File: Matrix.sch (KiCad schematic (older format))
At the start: 227 parts

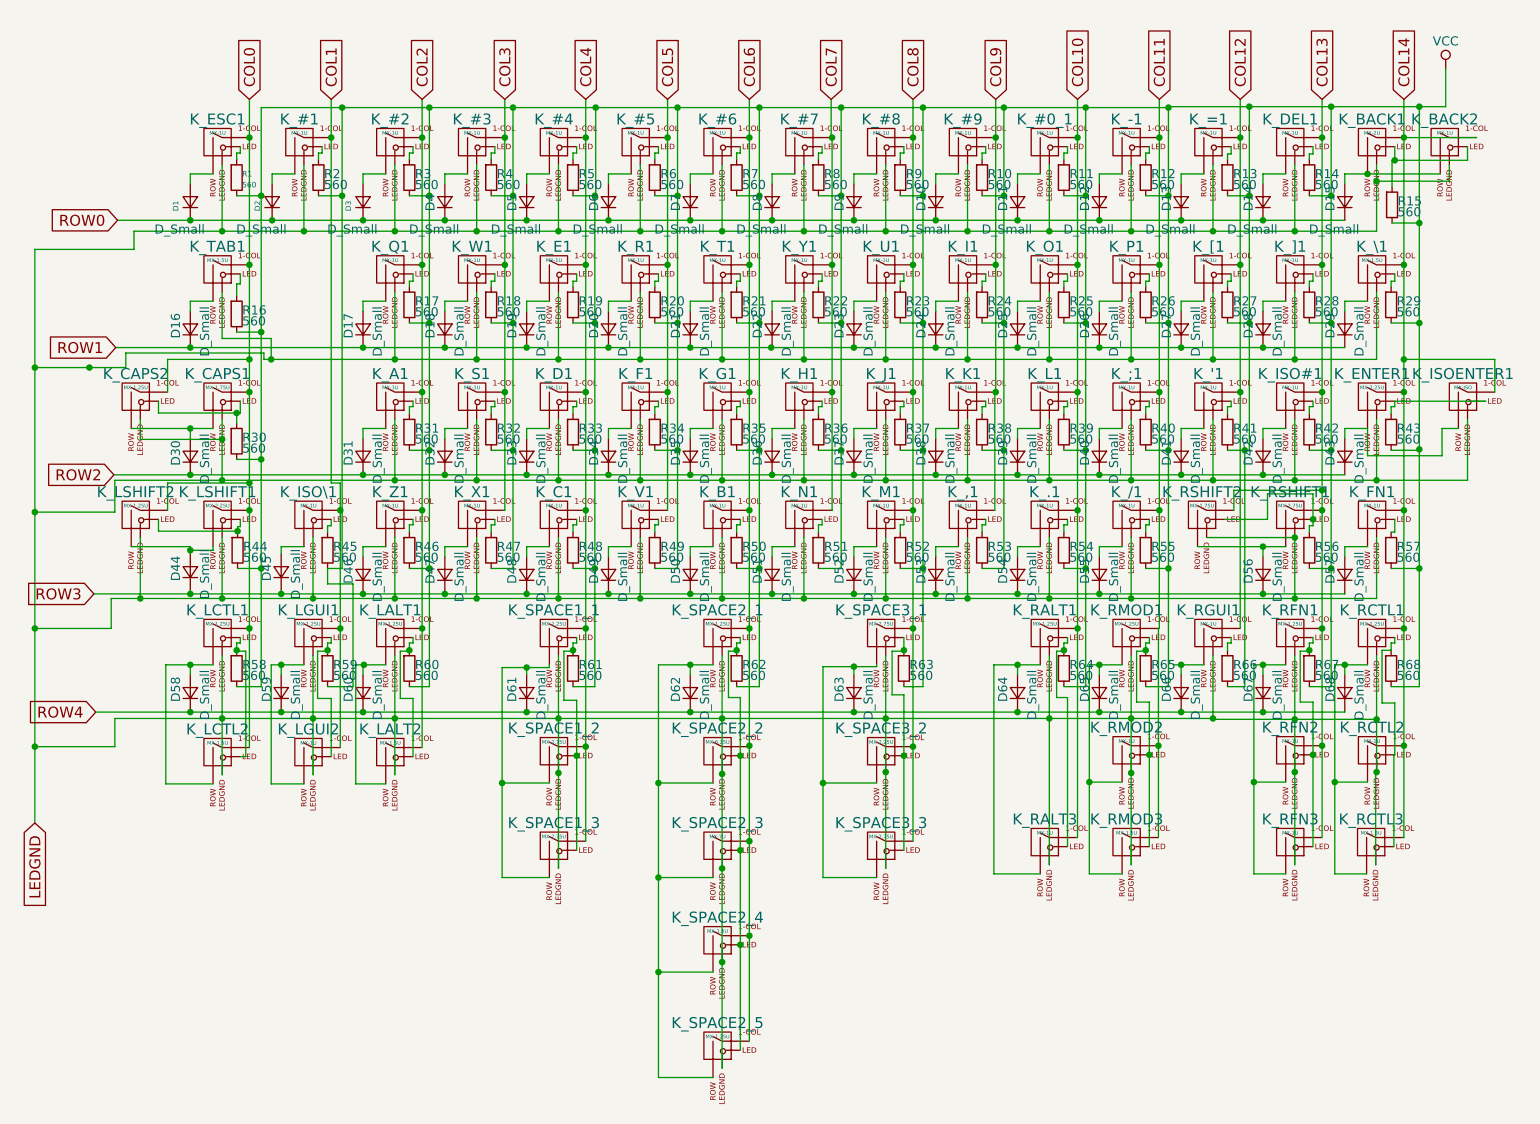
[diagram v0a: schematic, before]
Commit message: Update: Work on moving resistors in schematic. Not done yet.
I've got the top three rows done so far.
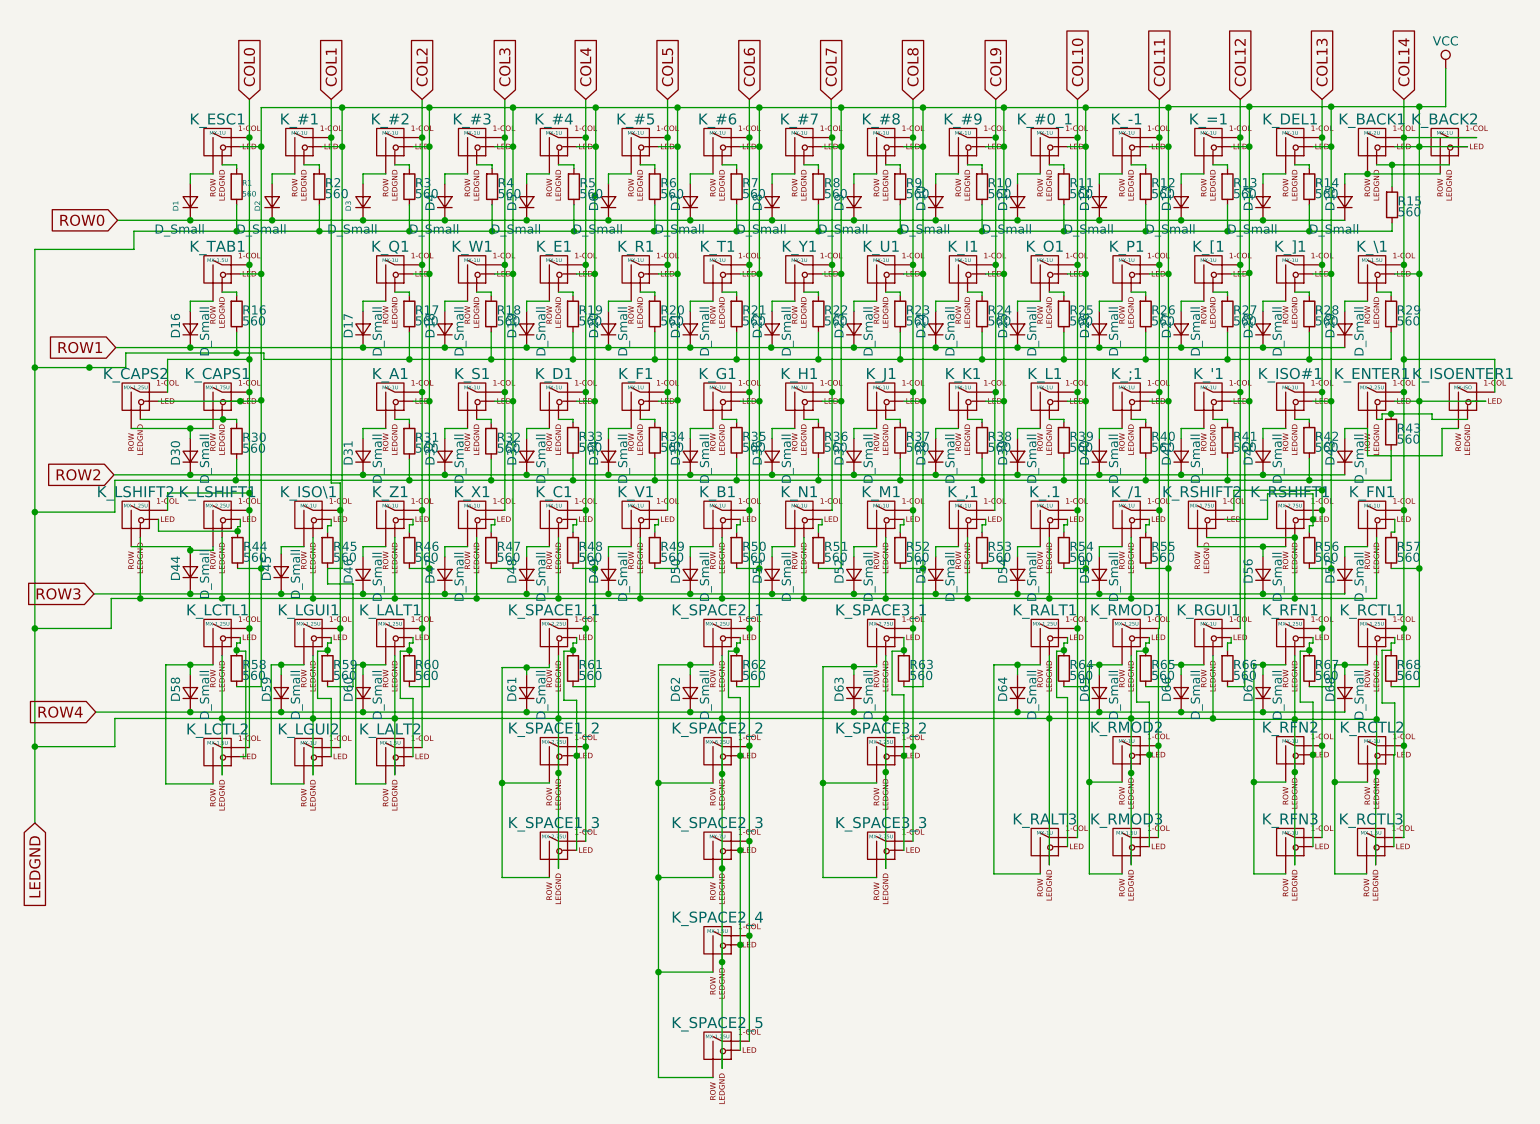
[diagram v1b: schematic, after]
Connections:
- net LEDGND: now also R1.2, R10.2, R11.2, R12.2, R13.2, R14.2, R15.2, R16.2, R17.2, R18.2, R19.2, R2.2, R20.2, R21.2, R22.2, R23.2, R24.2, R25.2, R26.2, R27.2, R28.2, R29.2, R3.2, R30.2, R31.2, R32.2, R33.2, R34.2, R35.2, R36.2, R37.2, R38.2, R39.2, R4.2, R40.2, R41.2, R42.2, R43.2, R5.2, R6.2, R7.2, R8.2, R9.2; no longer K_#0_1.4 (LEDGND), K_#1.4 (LEDGND), K_#2.4 (LEDGND), K_#3.4 (LEDGND), K_#4.4 (LEDGND), K_#5.4 (LEDGND), K_#6.4 (LEDGND), K_#7.4 (LEDGND), K_#8.4 (LEDGND), K_#9.4 (LEDGND), K_'1.4 (LEDGND), K_-1.4 (LEDGND), K_;1.4 (LEDGND), K_=1.4 (LEDGND), K_A1.4 (LEDGND), K_BACK1.4 (LEDGND), K_BACK2.4 (LEDGND), K_CAPS1.4 (LEDGND), K_CAPS2.4 (LEDGND), K_D1.4 (LEDGND), K_DEL1.4 (LEDGND), K_E1.4 (LEDGND), K_ENTER1.4 (LEDGND), K_ESC1.4 (LEDGND), K_F1.4 (LEDGND), K_G1.4 (LEDGND), K_H1.4 (LEDGND), K_I1.4 (LEDGND), K_ISO#1.4 (LEDGND), K_ISOENTER1.4 (LEDGND), K_J1.4 (LEDGND), K_K1.4 (LEDGND), K_L1.4 (LEDGND), K_O1.4 (LEDGND), K_P1.4 (LEDGND), K_Q1.4 (LEDGND), K_R1.4 (LEDGND), K_S1.4 (LEDGND), K_T1.4 (LEDGND), K_TAB1.4 (LEDGND), K_U1.4 (LEDGND), K_W1.4 (LEDGND), K_Y1.4 (LEDGND), K_[1.4 (LEDGND), K_\1.4 (LEDGND), K_]1.4 (LEDGND)
- net VCC: now also K_#0_1.3 (LED), K_#1.3 (LED), K_#2.3 (LED), K_#3.3 (LED), K_#4.3 (LED), K_#5.3 (LED), K_#6.3 (LED), K_#7.3 (LED), K_#8.3 (LED), K_#9.3 (LED), K_'1.3 (LED), K_-1.3 (LED), K_;1.3 (LED), K_=1.3 (LED), K_A1.3 (LED), K_BACK1.3 (LED), K_BACK2.3 (LED), K_CAPS1.3 (LED), K_CAPS2.3 (LED), K_DEL1.3 (LED), K_ENTER1.3 (LED), K_ESC1.3 (LED), K_F1.3 (LED), K_G1.3 (LED), K_H1.3 (LED), K_I1.3 (LED), K_ISO#1.3 (LED), K_ISOENTER1.3 (LED), K_J1.3 (LED), K_K1.3 (LED), K_L1.3 (LED), K_O1.3 (LED), K_P1.3 (LED), K_Q1.3 (LED), K_R1.3 (LED), K_S1.3 (LED), K_T1.3 (LED), K_TAB1.3 (LED), K_U1.3 (LED), K_W1.3 (LED), K_Y1.3 (LED), K_[1.3 (LED), K_\1.3 (LED), K_]1.3 (LED); no longer R1.2, R10.2, R11.2, R12.2, R13.2, R14.2, R15.2, R16.2, R17.2, R18.2, R19.2, R2.2, R20.2, R21.2, R22.2, R23.2, R24.2, R25.2, R26.2, R27.2, R28.2, R29.2, R3.2, R30.2, R31.2, R32.2, R33.2, R34.2, R35.2, R36.2, R37.2, R38.2, R39.2, R4.2, R40.2, R41.2, R42.2, R43.2, R48.2, R5.2, R6.2, R61.2, R7.2, R8.2, R9.2
- net at R1.1: now also K_ESC1.4 (LEDGND); no longer K_ESC1.3 (LED)
- net at R2.1: now also K_#1.4 (LEDGND); no longer K_#1.3 (LED)
- net at R3.1: now also K_#2.4 (LEDGND); no longer K_#2.3 (LED)
- net at R4.1: now also K_#3.4 (LEDGND); no longer K_#3.3 (LED)
- net at R5.1: now also K_#4.4 (LEDGND); no longer K_#4.3 (LED)
- net at R6.1: now also K_#5.4 (LEDGND); no longer K_#5.3 (LED)
- net at R7.1: now also K_#6.4 (LEDGND); no longer K_#6.3 (LED)
- net at R8.1: now also K_#7.4 (LEDGND); no longer K_#7.3 (LED)
- net at R9.1: now also K_#8.4 (LEDGND); no longer K_#8.3 (LED)
- net at R10.1: now also K_#9.4 (LEDGND); no longer K_#9.3 (LED)
- net at R11.1: now also K_#0_1.4 (LEDGND); no longer K_#0_1.3 (LED)
- net at R12.1: now also K_-1.4 (LEDGND); no longer K_-1.3 (LED)
- net at R13.1: now also K_=1.4 (LEDGND); no longer K_=1.3 (LED)
- net at R14.1: now also K_DEL1.4 (LEDGND); no longer K_DEL1.3 (LED)
- net at R16.1: now also K_TAB1.4 (LEDGND); no longer K_TAB1.3 (LED)
- net at R17.1: now also K_Q1.4 (LEDGND); no longer K_Q1.3 (LED)
- net at R18.1: now also K_W1.4 (LEDGND); no longer K_W1.3 (LED)
- net at K_E1.3 (LED): now also K_D1.3 (LED), R48.2, R61.2; no longer R19.1
- net at R20.1: now also K_R1.4 (LEDGND); no longer K_R1.3 (LED)
- net at R21.1: now also K_T1.4 (LEDGND); no longer K_T1.3 (LED)
- net at R22.1: now also K_Y1.4 (LEDGND); no longer K_Y1.3 (LED)
- net at R23.1: now also K_U1.4 (LEDGND); no longer K_U1.3 (LED)
- net at R24.1: now also K_I1.4 (LEDGND); no longer K_I1.3 (LED)
- net at R25.1: now also K_O1.4 (LEDGND); no longer K_O1.3 (LED)
- net at R26.1: now also K_P1.4 (LEDGND); no longer K_P1.3 (LED)
- net at R27.1: now also K_[1.4 (LEDGND); no longer K_[1.3 (LED)
- net at R28.1: now also K_]1.4 (LEDGND); no longer K_]1.3 (LED)
- net at R29.1: now also K_\1.4 (LEDGND); no longer K_\1.3 (LED)
- net at R31.1: now also K_A1.4 (LEDGND); no longer K_A1.3 (LED)
- net at R32.1: now also K_S1.4 (LEDGND); no longer K_S1.3 (LED)
- net at R33.1: now also K_D1.4 (LEDGND); no longer K_D1.3 (LED)
- net at R34.1: now also K_F1.4 (LEDGND); no longer K_F1.3 (LED)
- net at R35.1: now also K_G1.4 (LEDGND); no longer K_G1.3 (LED)
- net at R36.1: now also K_H1.4 (LEDGND); no longer K_H1.3 (LED)
- net at R37.1: now also K_J1.4 (LEDGND); no longer K_J1.3 (LED)
- net at R38.1: now also K_K1.4 (LEDGND); no longer K_K1.3 (LED)
- net at R39.1: now also K_L1.4 (LEDGND); no longer K_L1.3 (LED)
- net at R40.1: now also K_;1.4 (LEDGND); no longer K_;1.3 (LED)
- net at R41.1: now also K_'1.4 (LEDGND); no longer K_'1.3 (LED)
- net at R42.1: now also K_ISO#1.4 (LEDGND); no longer K_ISO#1.3 (LED)
- new net: K_BACK1.4 (LEDGND), K_BACK2.4 (LEDGND), R15.1
- new net: K_E1.4 (LEDGND), R19.1
- new net: K_CAPS1.4 (LEDGND), K_CAPS2.4 (LEDGND), R30.1
- new net: K_ENTER1.4 (LEDGND), K_ISOENTER1.4 (LEDGND), R43.1
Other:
- moved on the sheet: R1, R10, R11, R12, R13, R14, R17, R18, R19, R2, R20, R21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

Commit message: Update: Finish moving resistors to ground side
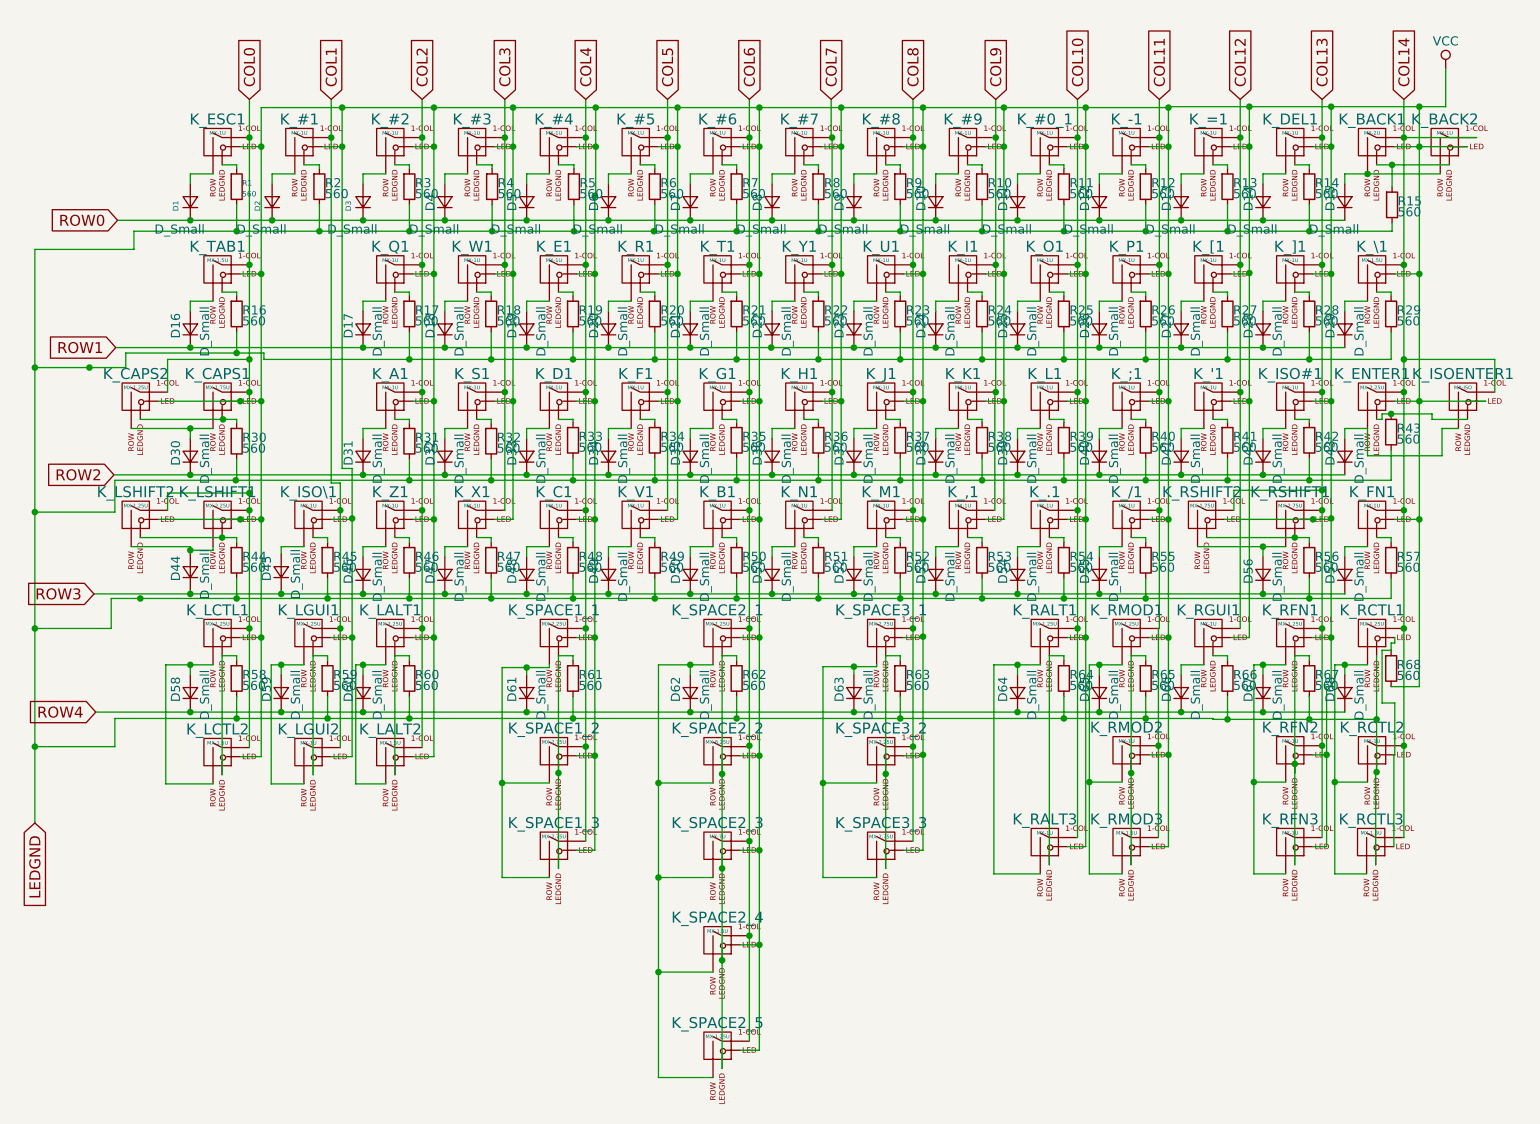
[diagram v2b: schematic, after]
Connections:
- net LEDGND: now also R44.2, R45.2, R46.2, R47.2, R48.2, R49.2, R50.2, R51.2, R52.2, R53.2, R54.2, R55.2, R56.2, R57.2, R58.2, R59.2, R60.2, R61.2, R62.2, R63.2, R64.2, R65.2, R66.2, R67.2; no longer K_,1.4 (LEDGND), K_.1.4 (LEDGND), K_/1.4 (LEDGND), K_B1.4 (LEDGND), K_C1.4 (LEDGND), K_FN1.4 (LEDGND), K_ISO\1.4 (LEDGND), K_LALT1.4 (LEDGND), K_LALT2.4 (LEDGND), K_LCTL1.4 (LEDGND), K_LCTL2.4 (LEDGND), K_LGUI1.4 (LEDGND), K_LGUI2.4 (LEDGND), K_LSHIFT1.4 (LEDGND), K_LSHIFT2.4 (LEDGND), K_M1.4 (LEDGND), K_N1.4 (LEDGND), K_RALT1.4 (LEDGND), K_RALT3.4 (LEDGND), K_RFN1.4 (LEDGND), K_RFN2.4 (LEDGND), K_RFN3.4 (LEDGND), K_RGUI1.4 (LEDGND), K_RMOD1.4 (LEDGND), K_RMOD2.4 (LEDGND), K_RMOD3.4 (LEDGND), K_RSHIFT1.4 (LEDGND), K_RSHIFT2.4 (LEDGND), K_SPACE1_1.4 (LEDGND), K_SPACE1_2.4 (LEDGND), K_SPACE1_3.4 (LEDGND), K_SPACE2_1.4 (LEDGND), K_SPACE2_2.4 (LEDGND), K_SPACE2_3.4 (LEDGND), K_SPACE2_4.4 (LEDGND), K_SPACE2_5.4 (LEDGND), K_SPACE3_1.4 (LEDGND), K_SPACE3_2.4 (LEDGND), K_SPACE3_3.4 (LEDGND), K_V1.4 (LEDGND), K_X1.4 (LEDGND), K_Z1.4 (LEDGND)
- net VCC: now also K_,1.3 (LED), K_.1.3 (LED), K_/1.3 (LED), K_B1.3 (LED), K_FN1.3 (LED), K_ISO\1.3 (LED), K_LALT1.3 (LED), K_LALT2.3 (LED), K_LCTL1.3 (LED), K_LCTL2.3 (LED), K_LGUI1.3 (LED), K_LGUI2.3 (LED), K_LSHIFT1.3 (LED), K_LSHIFT2.3 (LED), K_M1.3 (LED), K_N1.3 (LED), K_RALT1.3 (LED), K_RALT3.3 (LED), K_RFN1.3 (LED), K_RFN2.3 (LED), K_RFN3.3 (LED), K_RGUI1.3 (LED), K_RMOD1.3 (LED), K_RMOD2.3 (LED), K_RMOD3.3 (LED), K_RSHIFT1.3 (LED), K_RSHIFT2.3 (LED), K_SPACE2_1.3 (LED), K_SPACE2_2.3 (LED), K_SPACE2_3.3 (LED), K_SPACE2_4.3 (LED), K_SPACE2_5.3 (LED), K_SPACE3_1.3 (LED), K_SPACE3_2.3 (LED), K_SPACE3_3.3 (LED), K_V1.3 (LED), K_X1.3 (LED), K_Z1.3 (LED); no longer R44.2, R45.2, R46.2, R47.2, R49.2, R50.2, R51.2, R52.2, R53.2, R54.2, R55.2, R56.2, R57.2, R58.2, R59.2, R60.2, R62.2, R63.2, R64.2, R65.2, R66.2, R67.2
- net at K_D1.3 (LED), K_E1.3 (LED): now also K_C1.3 (LED), K_SPACE1_1.3 (LED), K_SPACE1_2.3 (LED), K_SPACE1_3.3 (LED); no longer R48.2, R61.2
- net at R45.1: now also K_ISO\1.4 (LEDGND); no longer K_ISO\1.3 (LED)
- net at R46.1: now also K_Z1.4 (LEDGND); no longer K_Z1.3 (LED)
- net at R47.1: now also K_X1.4 (LEDGND); no longer K_X1.3 (LED)
- net at R48.1: now also K_C1.4 (LEDGND); no longer K_C1.3 (LED)
- net at R49.1: now also K_V1.4 (LEDGND); no longer K_V1.3 (LED)
- net at R50.1: now also K_B1.4 (LEDGND); no longer K_B1.3 (LED)
- net at R51.1: now also K_N1.4 (LEDGND); no longer K_N1.3 (LED)
- net at R52.1: now also K_M1.4 (LEDGND); no longer K_M1.3 (LED)
- net at R53.1: now also K_,1.4 (LEDGND); no longer K_,1.3 (LED)
- net at R54.1: now also K_.1.4 (LEDGND); no longer K_.1.3 (LED)
- net at R55.1: now also K_/1.4 (LEDGND); no longer K_/1.3 (LED)
- net at R57.1: now also K_FN1.4 (LEDGND); no longer K_FN1.3 (LED)
- net at R66.1: now also K_RGUI1.4 (LEDGND); no longer K_RGUI1.3 (LED)
- new net: K_LSHIFT1.4 (LEDGND), K_LSHIFT2.4 (LEDGND), R44.1
- new net: K_RSHIFT1.4 (LEDGND), K_RSHIFT2.4 (LEDGND), R56.1
- new net: K_LCTL1.4 (LEDGND), K_LCTL2.4 (LEDGND), R58.1
- new net: K_LGUI1.4 (LEDGND), K_LGUI2.4 (LEDGND), R59.1
- new net: K_LALT1.4 (LEDGND), K_LALT2.4 (LEDGND), R60.1
- new net: K_SPACE1_1.4 (LEDGND), K_SPACE1_2.4 (LEDGND), K_SPACE1_3.4 (LEDGND), R61.1
- new net: K_SPACE2_1.4 (LEDGND), K_SPACE2_2.4 (LEDGND), K_SPACE2_3.4 (LEDGND), K_SPACE2_4.4 (LEDGND), K_SPACE2_5.4 (LEDGND), R62.1
- new net: K_SPACE3_1.4 (LEDGND), K_SPACE3_2.4 (LEDGND), K_SPACE3_3.4 (LEDGND), R63.1
- new net: K_RALT1.4 (LEDGND), K_RALT3.4 (LEDGND), R64.1
- new net: K_RMOD1.4 (LEDGND), K_RMOD2.4 (LEDGND), K_RMOD3.4 (LEDGND), R65.1
- new net: K_RFN1.4 (LEDGND), K_RFN2.4 (LEDGND), K_RFN3.4 (LEDGND), R67.1
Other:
- moved on the sheet: R44, R45, R46, R47, R48, R49, R50, R51, R52, R53, R54, R55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

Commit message: Update: Switch to Amphenol USB C connector
This connector seems more readily available than the Wurth,
and is about half the price.
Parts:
- K_ISOENTER1: footprint MX_Alps_Hybrid:MXOnly-ISO-ReversedStabilizers -> MX_Alps_Hybrid:MXOnly-ISO-ROTATED-ReversedStabilizers
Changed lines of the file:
@@
 F 0 "K_ISOENTER1" H 8400 2625 60  0000 C CNN
 F 1 "MX-ISO" H 8400 2550 20  0000 C CNN
-F 2 "MX_Alps_Hybrid:MXOnly-ISO-ReversedStabilizers" H 8375 2475 60  0001 C CNN
+F 2 "MX_Alps_Hybrid:MXOnly-ISO-ROTATED-ReversedStabilizers" H 8375 2475 60  0001 C CNN
 F 3 "" H 8375 2475 60  0001 C CNN
 	1    8400 2500

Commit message: Update: Choose more components, lock switch footprints, place some resistors and diodes
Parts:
- D1: Product (none) -> 1N4148W-TP
- R1: Product (none) -> MCT06030C5600FP500
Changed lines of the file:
@@
 F 1 "D_Small" V 1250 1350 50  0000 L CNN
 F 2 "Diodes_SMD:D_SOD-123" V 1400 1430 50  0001 C CNN
-F 3 "" V 1400 1430 50  0001 C CNN
+F 3 "http://www.mccsemi.com/up_pdf/1N4148W(SOD123).pdf" V 1400 1430 50  0001 C CNN
+F 4 "1N4148W-TP" H 1400 1430 60  0001 C CNN "Product"
 	1    1400 1430
 	0    -1   -1   0
@@
 F 2 "Resistors_SMD:R_0603" H 1655 1345 50  0001 C CNN
 F 3 "" H 1655 1345 50  0001 C CNN
+F 4 "MCT06030C5600FP500" H 1655 1345 60  0001 C CNN "Product"
 	1    1655 1345
 	1    0    0    -1

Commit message: Update: Flip LED orientation on most switch footprints
I'm hoping this will separate the diodes and resistors
a little more and make routing easier.
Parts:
- K_#0_1, K_#1, K_#2, K_#3, K_#4, K_#5, K_#6, K_#7, K_#8, K_#9, K_'1, K_,1, K_-1, K_.1, K_/1, K_;1, K_=1, K_A1, K_B1, K_BACK2, K_C1, K_D1, K_DEL1, K_E1, K_ESC1, K_F1, K_FN1, K_G1, K_H1, K_I1, K_ISO#1, K_ISO\1, K_J1, K_K1, K_L1, K_M1, K_N1, K_O1, K_P1, K_Q1, K_R1, K_RGUI1, K_S1, K_T1, K_U1, K_V1, K_W1, K_X1, K_Y1, K_Z1, K_[1, K_]1: footprint MX_Alps_Hybrid:MXOnly-1U -> MX_Alps_Hybrid:MXOnly-1U-FLIPPED
- K_BACK1: footprint MX_Alps_Hybrid:MXOnly-2U -> MX_Alps_Hybrid:MXOnly-2U-FLIPPED
- K_ENTER1, K_LSHIFT1: footprint MX_Alps_Hybrid:MXOnly-2.25U -> MX_Alps_Hybrid:MXOnly-2.25U-FLIPPED
- K_LSHIFT2: footprint MX_Alps_Hybrid:MXOnly-1.25U -> MX_Alps_Hybrid:MXOnly-1.25U-FLIPPED
- K_RSHIFT1: footprint MX_Alps_Hybrid:MXOnly-2.75U -> MX_Alps_Hybrid:MXOnly-2.75U-FLIPPED
- K_RSHIFT2: footprint MX_Alps_Hybrid:MXOnly-1.75U -> MX_Alps_Hybrid:MXOnly-1.75U-FLIPPED
- K_TAB1, K_\1: footprint MX_Alps_Hybrid:MXOnly-1.5U -> MX_Alps_Hybrid:MXOnly-1.5U-FLIPPED

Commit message: Update: More PCB component adjustment
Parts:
- K_LCTL1: footprint MX_Alps_Hybrid:MXOnly-1.25U -> MX_Alps_Hybrid:MXOnly-1.25U-FLIPPED
- K_LCTL2: footprint MX_Alps_Hybrid:MXOnly-1.5U-FLIPPED -> MX_Alps_Hybrid:MXOnly-1.5U
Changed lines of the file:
@@
 F 0 "K_LCTL1" H 1550 3925 60  0000 C CNN
 F 1 "MX-1.25U" H 1550 3850 20  0000 C CNN
-F 2 "MX_Alps_Hybrid:MXOnly-1.25U" H 1525 3775 60  0001 C CNN
+F 2 "MX_Alps_Hybrid:MXOnly-1.25U-FLIPPED" H 1525 3775 60  0001 C CNN
 F 3 "" H 1525 3775 60  0001 C CNN
 	1    1550 3800
@@
 F 0 "K_LCTL2" H 1550 4580 60  0000 C CNN
 F 1 "MX-1.5U" H 1550 4505 20  0000 C CNN
-F 2 "MX_Alps_Hybrid:MXOnly-1.5U-FLIPPED" H 1525 4430 60  0001 C CNN
+F 2 "MX_Alps_Hybrid:MXOnly-1.5U" H 1525 4430 60  0001 C CNN
 F 3 "" H 1525 4430 60  0001 C CNN
 	1    1550 4455
